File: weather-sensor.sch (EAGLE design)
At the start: 47 parts, among them J1 43841-0005, J2 95501-6889, U1 SHT31, U2 MPL3115A2LGA8, U5 MIC5219-3.3YM5-TR, U6 PCA9615

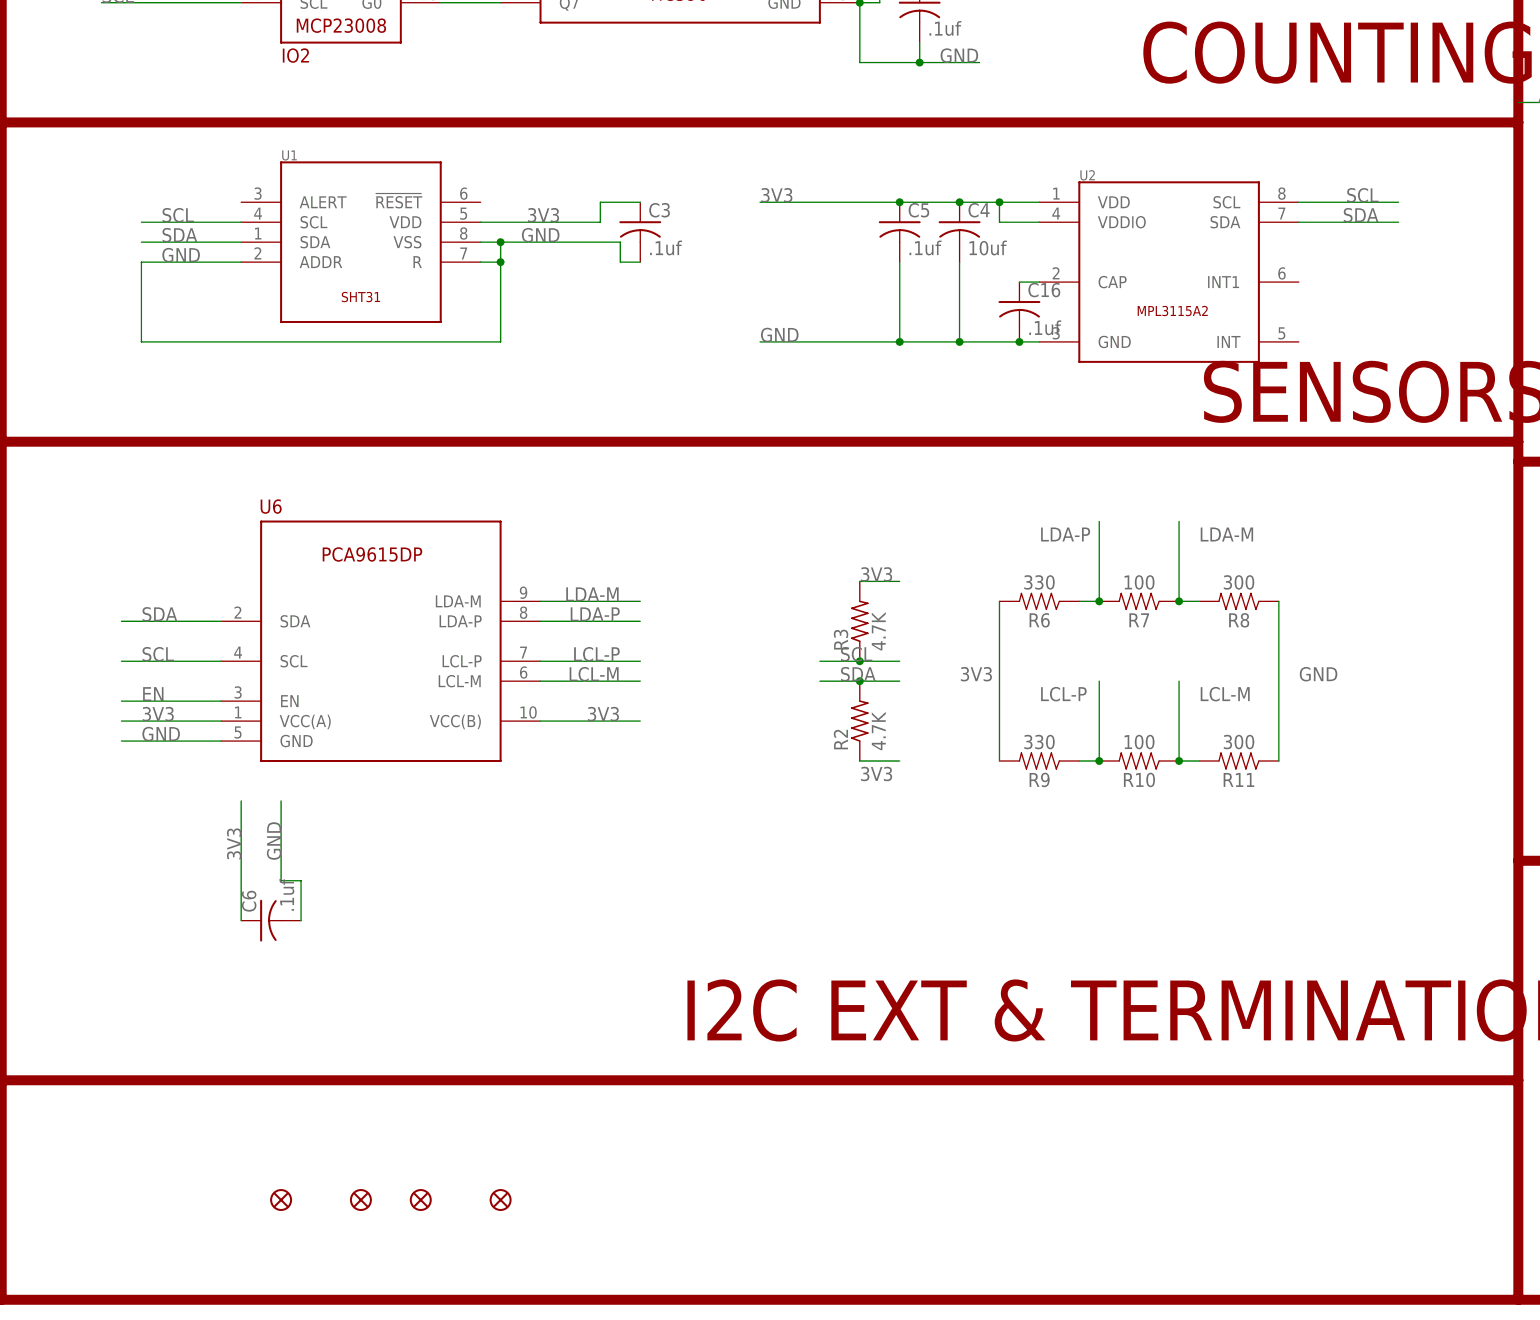
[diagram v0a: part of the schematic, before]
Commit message: Replaced sensors with BME280, Reworked outline for compatibility with new arm.
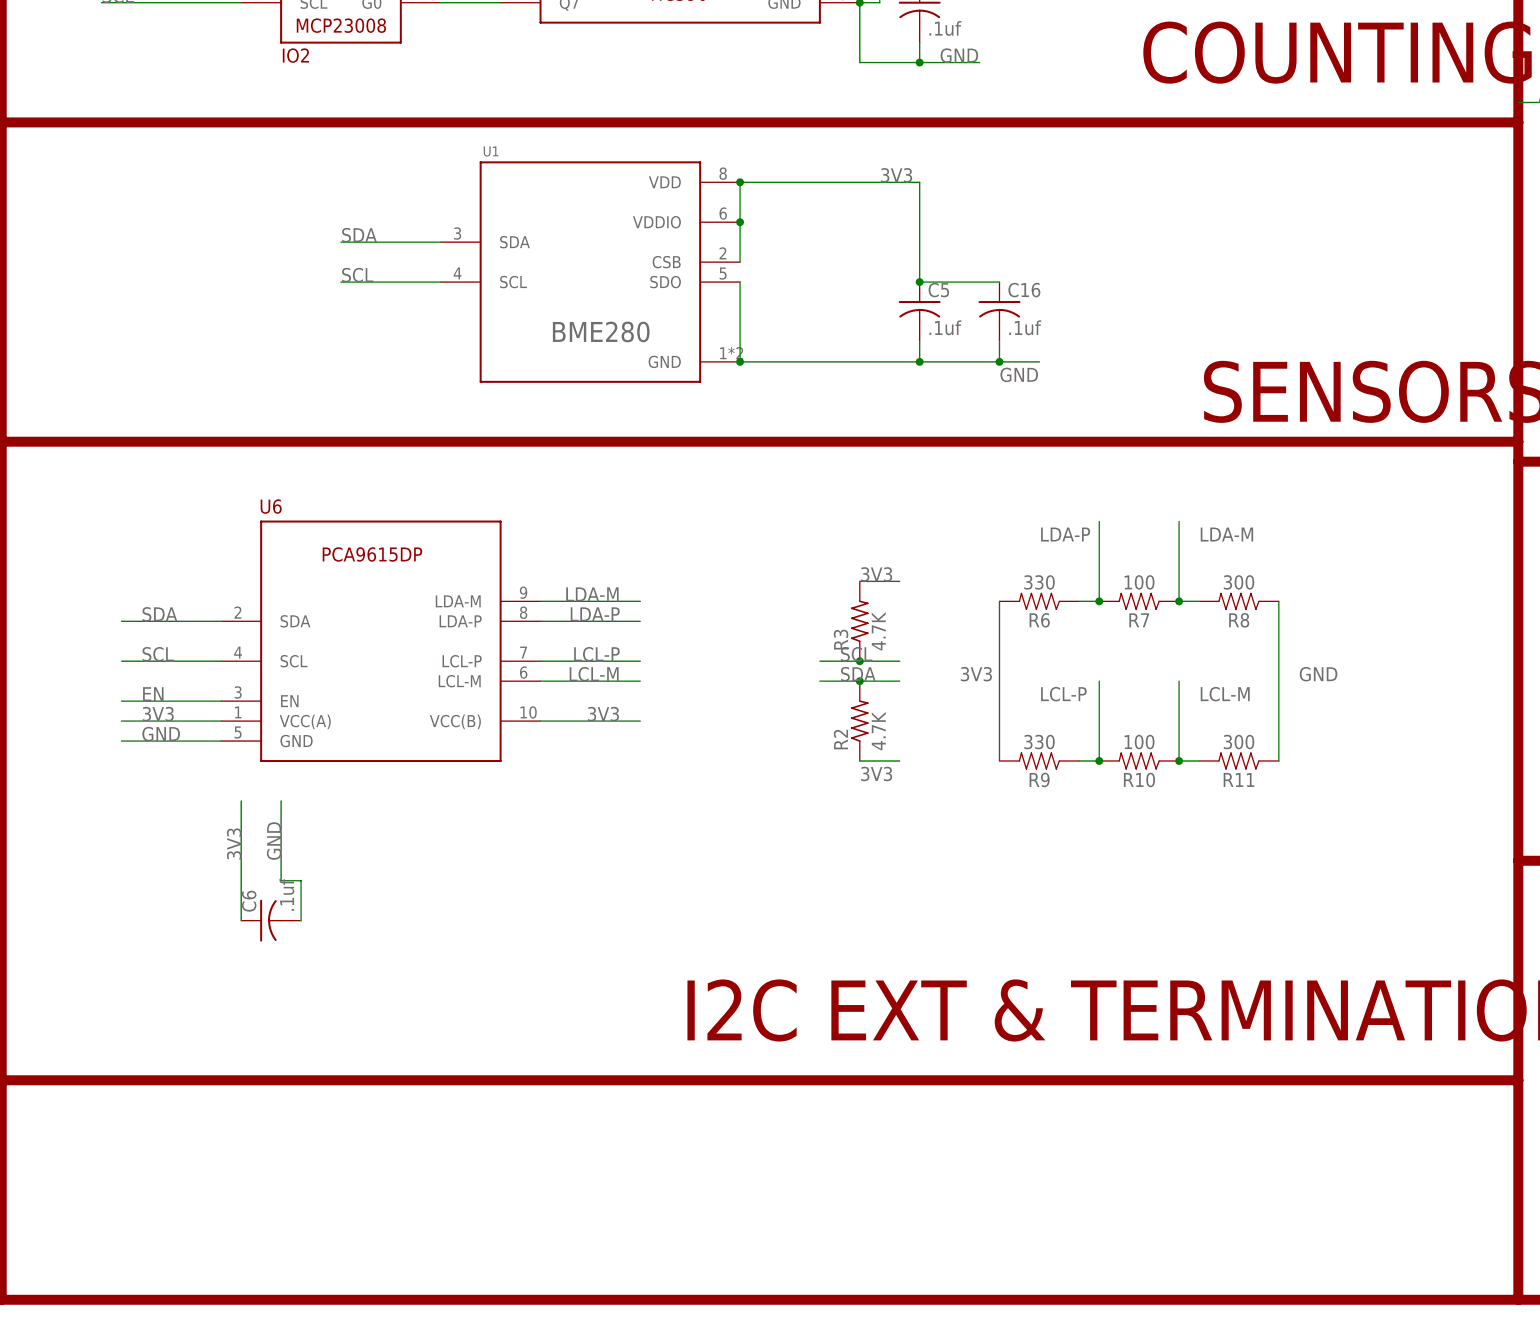
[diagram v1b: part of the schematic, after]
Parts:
- removed C3: .1uf, rcl:C-USC0603K
- removed C4: 10uf, rcl:C-USC0603K
- removed FID1, FID2, FID3, FID4: FIDUCIAL1X2.5, microbuilder:FIDUCIAL1X2.5
- removed U2: MPL3115A2LGA8, Conservify:MPL3115A2LGA8
- U1: value SHT31 -> BME280; device Conservify:SHT31 -> Conservify:BME280
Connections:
- removed net CAP: C16.1, U2.CAP
- net 3V3: now also C16.1, U1.CSB, U1.VDDIO; no longer C3.1, C4.1, U2.VDD, U2.VDDIO
- net GND: now also U1.GND, U1.SDO; no longer C3.2, C4.2, U1.ADDR, U1.R, U1.VSS, U2.GND
- net SCL: no longer U2.SCL
- net SDA: no longer U2.SDA
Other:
- moved on the sheet: C16, C5
